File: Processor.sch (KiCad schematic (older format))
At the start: 6 parts, among them J10 B4B-ZR, J9 2309411-1, U13 TXS0102DCUR

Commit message: PVT
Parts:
- removed J10: B4B-ZR, Connector-JST:B4B-ZR, symbol Connector_Generic:Conn_01x04
- removed U13: TXS0102DCUR, IC-SOP:VSSOP8, symbol interface-ti:TXS0102DCU
- added RA1: 4.7k, Resistor-Chip:R_CHIP_4x1005_CONCAVE, symbol passive:R_Array_4
- added TP24: PWM, Print:TP_C1.0, symbol print:TestPoint
- added TP25: TACHO, Print:TP_C1.0, symbol print:TestPoint
- added U11: DNP(AT24C02D-XHM-T), IC-SOP:TSSOP8_W4.4, symbol memory-microchip:AT24C0xD-8PIN
- renumbered R58 to R51
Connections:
- net +1V8: now also RA1.C1, U11.1 (A0), U11.2 (A1), U11.3 (A2), U11.8 (VCC)
- net GND: now also U11.4 (GND), U11.7 (WP)
- net GPIO08_FAN_TACHO: now also TP25.1
- net GPIO14_FAN_PWM: now also TP24.1
- net I2C2_SCL: now also U11.6 (SCL)
- net I2C2_SDA: now also U11.5 (SDA)
- net at J9.100 (DP1_AUX_P): now also RA1.B2
- net at J9.96 (DP1_HPD): now also RA1.C2
- net at J9.98 (DP1_AUX_N): now also RA1.A2
- net CAN_RX: no longer names the net of J9.143 (NC(CAN_RX))
- net CAN_TX: no longer names the net of J9.145 (NC(CAN_TX))
- net I2S1_DIN: no longer names the net of J9.222 (I2S1_DIN)
- net I2S1_DOUT: no longer names the net of J9.220 (I2S1_DOUT)
- net I2S1_FS: no longer names the net of J9.224 (I2S1_FS)
- net I2S1_SCLK: no longer names the net of J9.226 (I2S1_SCLK)
- net UART2_RXD: no longer names the net of J9.238 (UART2_RXD)
- net UART2_TXD: no longer names the net of J9.236 (UART2_TXD)
- net ~UART0_CTS: no longer names the net of J9.105 (~UART0_CTS)
- net ~UART0_RTS: no longer names the net of J9.103 (~UART0_RTS)
- new net +3V3: RA1.A1, RA1.B1
- no-connect marks 57 -> 62
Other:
- note removed: "Fan Controller"
- moved on the sheet: J9H

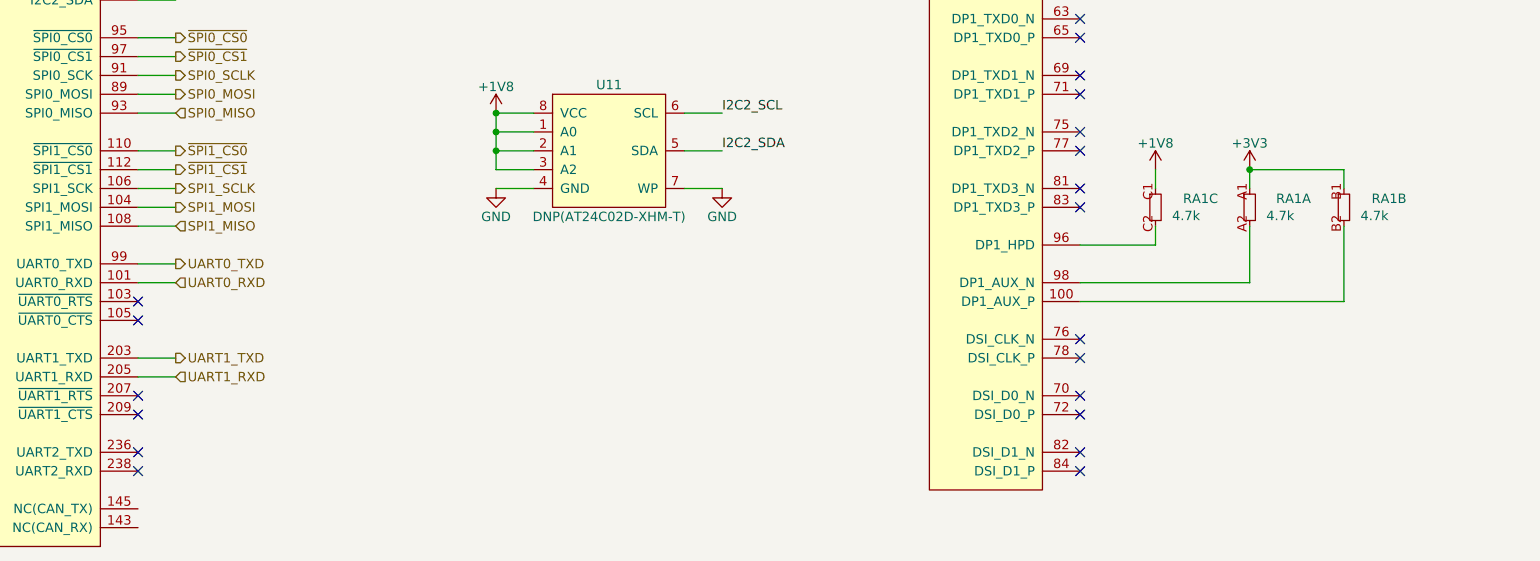
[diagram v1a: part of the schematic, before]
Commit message: SBUにTVSダイオードを追加
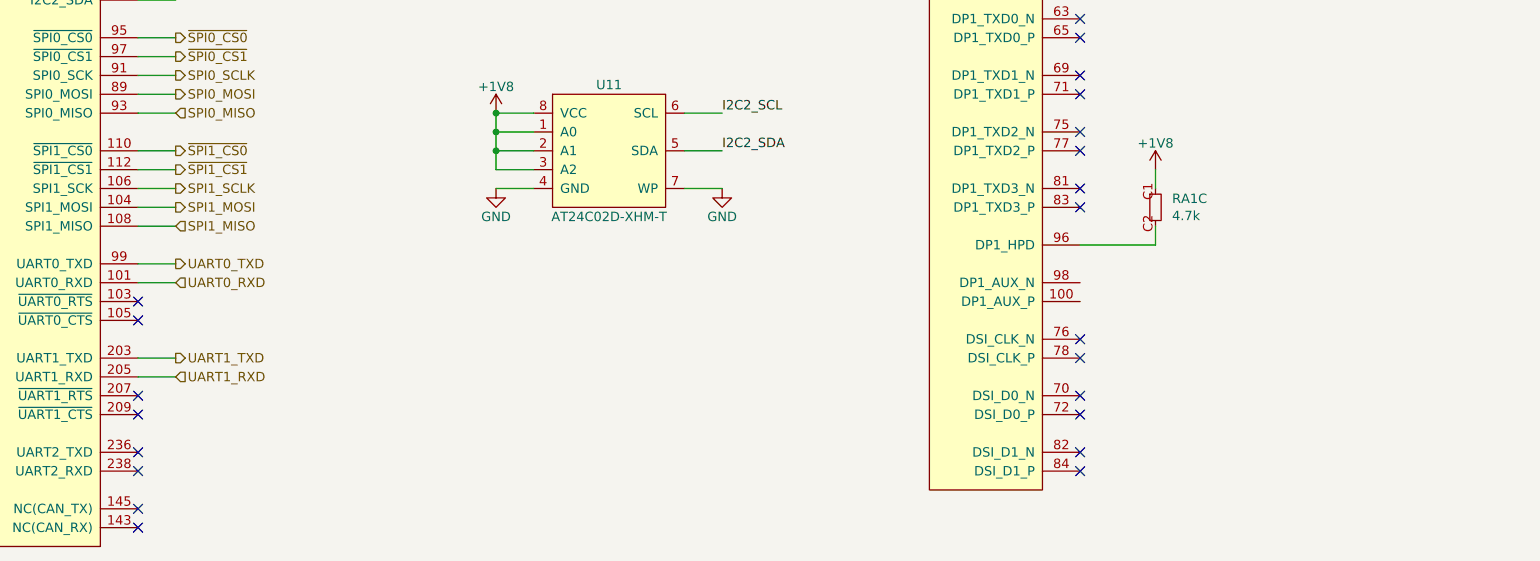
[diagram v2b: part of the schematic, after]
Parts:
- removed unit 1 of RA1
- removed unit 2 of RA1
- U11: value DNP(AT24C02D-XHM-T) -> AT24C02D-XHM-T
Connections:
- no-connect marks 62 -> 64
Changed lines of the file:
@@
 $EndComp
 $Comp
-L supply-alias:GND #PWR0170
+L supply-alias:GND #PWR0169
 U 1 1 5EA21E39
 P 15800 8600
-F 0 "#PWR0170" H 15800 8350 50  0001 C CNN
+F 0 "#PWR0169" H 15800 8350 50  0001 C CNN
 F 1 "GND" H 15800 8450 50  0000 C CNN
 F 2 "" H 15800 8600 50  0001 C CNN
@@
 Connection ~ 15800 8600
 $Comp
-L supply-value:+5V #PWR0168
+L supply-value:+5V #PWR0167
 U 1 1 5EA54343
 P 14200 2000
-F 0 "#PWR0168" H 14200 1850 50  0001 C CNN
+F 0 "#PWR0167" H 14200 1850 50  0001 C CNN
 F 1 "+5V" H 14200 2140 50  0000 C CNN
 F 2 "" H 14200 2000 50  0001 C CNN
@@
 Connection ~ 14200 2000
 $Comp
-L supply-alias:GND #PWR0169
+L supply-alias:GND #PWR0168
 U 1 1 5EA8F5AE
 P 14200 8600
-F 0 "#PWR0169" H 14200 8350 50  0001 C CNN
+F 0 "#PWR0168" H 14200 8350 50  0001 C CNN
 F 1 "GND" H 14200 8450 50  0000 C CNN
 F 2 "" H 14200 8600 50  0001 C CNN
@@
 NoConn ~ 2000 3200
 NoConn ~ 2000 3300
-$Sheet
-S 11000 1600 1000 1900
-U 5EE65BF3
-F0 "Processor-USBC2" 50
-F1 "Processor-USBC2.sch" 50
-F2 "USB_D-" B R 12000 1700 50
-F3 "USB_D+" B R 12000 1800 50
-F4 "USBSS_RX+" O R 12000 2400 50
-F5 "USBSS_RX-" O R 12000 2300 50
-F6 "USBSS_TX+" I R 12000 2700 50
-F7 "USBSS_TX-" I R 12000 2600 50
-F8 "DP_ML0+" I L 11000 1800 50
-F9 "DP_ML0-" I L 11000 1700 50
-F10 "DP_ML1+" I L 11000 2100 50
-F11 "DP_ML1-" I L 11000 2000 50
-F12 "DP_ML2+" I L 11000 2400 50
-F13 "DP_ML2-" I L 11000 2300 50
-F14 "DP_ML3+" I L 11000 2700 50
-F15 "DP_ML3-" I L 11000 2600 50
-F16 "DP_HPD" O L 11000 3200 50
-F17 "DP_AUX+" B L 11000 3000 50
-F18 "DP_AUX-" B L 11000 2900 50
-$EndSheet
 $Sheet
 S 11000 800  1000 300
@@
 Wire Wire Line
 	7400 9500 7400 9400
-Wire Wire Line
-	7900 9400 7900 9700
-Wire Wire Line
-	7900 9700 7000 9700
-Wire Wire Line
-	7000 9800 8400 9800
-Wire Wire Line
-	8400 9800 8400 9400
 $Comp
 L supply-value:+1V8 #PWR0166
@@
 	1    0    0    -1
 $EndComp
-$Comp
-L supply-value:+3V3 #PWR0167
-U 1 1 5F20E491
-P 7900 9100
-F 0 "#PWR0167" H 7900 8950 50  0001 C CNN
-F 1 "+3V3" H 7900 9240 50  0000 C CNN
-F 2 "" H 7900 9100 50  0001 C CNN
-F 3 "" H 7900 9100 50  0001 C CNN
-	1    7900 9100
-	1    0    0    -1
-$EndComp
-Wire Wire Line
-	7900 9100 7900 9200
-Wire Wire Line
-	7900 9100 8400 9100
-Wire Wire Line
-	8400 9100 8400 9200
-Connection ~ 7900 9100
 Wire Wire Line
 	7400 9100 7400 9200
-$Comp
-L passive:R_Array_4 RA?
-U 1 1 5F3A4A6E
-P 7900 9300
-AR Path="/5E4B5B3E/5F3A4A6E" Ref="RA?"  Part="4"
-AR Path="/5E4B5786/5F3A4A6E" Ref="RA?"  Part="4"
-AR Path="/5F235278/5F3A4A6E" Ref="RA?"  Part="1"
-AR Path="/5F235A43/5F3A4A6E" Ref="RA?"  Part="4"
-AR Path="/5E9E174E/5F3A4A6E" Ref="RA1"  Part="1"
-F 0 "RA1" H 8225 9346 50  0000 R CNN
-F 1 "4.7k" H 7988 9255 50  0000 L CNN
-F 2 "Resistor-Chip:R_CHIP_4x1005_CONCAVE" H 7900 9300 50  0001 C CNN
-F 3 "" H 7900 9300 50  0001 C CNN
-F 4 "EXB-N8V472JX" H 7900 9300 50  0001 C CNN "PartName"
-	1    7900 9300
-	1    0    0    -1
-$EndComp
-$Comp
-L passive:R_Array_4 RA?
-U 2 1 5F3A4A75
-P 8400 9300
-AR Path="/5E4B5B3E/5F3A4A75" Ref="RA?"  Part="2"
-AR Path="/5E4B5786/5F3A4A75" Ref="RA?"  Part="2"
-AR Path="/5F235278/5F3A4A75" Ref="RA?"  Part="3"
-AR Path="/5F235A43/5F3A4A75" Ref="RA?"  Part="3"
-AR Path="/5E9E174E/5F3A4A75" Ref="RA1"  Part="2"
-F 0 "RA1" H 8732 9346 50  0000 R CNN
-F 1 "4.7k" H 8488 9255 50  0000 L CNN
-F 2 "Resistor-Chip:R_CHIP_4x1005_CONCAVE" H 8400 9300 50  0001 C CNN
-F 3 "" H 8400 9300 50  0001 C CNN
-F 4 "EXB-N8V472JX" H 8400 9300 50  0001 C CNN "PartName"
-	2    8400 9300
-	1    0    0    -1
-$EndComp
 $Comp
 L passive:R_Array_4 RA?
@@
 AR Path="/5F235A43/5F3A4A7C" Ref="RA?"  Part="2"
 AR Path="/5E9E174E/5F3A4A7C" Ref="RA1"  Part="3"
-F 0 "RA1" H 7732 9346 50  0000 R CNN
+F 0 "RA1" H 7488 9346 50  0000 L CNN
 F 1 "4.7k" H 7488 9255 50  0000 L CNN
 F 2 "Resistor-Chip:R_CHIP_4x1005_CONCAVE" H 7400 9300 50  0001 C CNN
@@
 P 4500 9000
 F 0 "U11" H 4500 9350 50  0000 C CNN
-F 1 "DNP(AT24C02D-XHM-T)" H 4500 8650 50  0000 C CNN
+F 1 "AT24C02D-XHM-T" H 4500 8650 50  0000 C CNN
 F 2 "IC-SOP:TSSOP8_W4.4" H 4500 9000 50  0001 C CNN
 F 3 "" H 4500 9000 50  0001 C CNN
@@
 Wire Wire Line
 	4700 7600 4900 7600
+NoConn ~ 2000 10900
+NoConn ~ 2000 11000
+$Sheet
+S 11000 1600 1000 1900
+U 5EE65BF3
+F0 "Processor-USBC2" 50
+F1 "Processor-USBC2.sch" 50
+F2 "USB_D-" B R 12000 1700 50
+F3 "USB_D+" B R 12000 1800 50
+F4 "USBSS_RX+" O R 12000 2400 50
+F5 "USBSS_RX-" O R 12000 2300 50
+F6 "USBSS_TX+" I R 12000 2700 50
+F7 "USBSS_TX-" I R 12000 2600 50
+F8 "DP_ML0+" I L 11000 1800 50
+F9 "DP_ML0-" I L 11000 1700 50
+F10 "DP_ML1+" I L 11000 2100 50
+F11 "DP_ML1-" I L 11000 2000 50
+F12 "DP_ML2+" I L 11000 2400 50
+F13 "DP_ML2-" I L 11000 2300 50
+F14 "DP_ML3+" I L 11000 2700 50
+F15 "DP_ML3-" I L 11000 2600 50
+F16 "DP_HPD" O L 11000 3200 50
+F17 "DP_AUX+" B L 11000 3000 50
+F18 "DP_AUX-" B L 11000 2900 50
+$EndSheet
 $EndSCHEMATC
